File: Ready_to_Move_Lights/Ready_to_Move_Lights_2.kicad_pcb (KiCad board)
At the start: 2 copper layers, 81.3 x 81.3 mm, 46 parts, among them IC1 TLV2371QDBVRQ1, J1 PET-02-XX-X-VT-LC, J2 776280-1, K1 VORA1150-X017T, Q1 IRLZ44N, U1 LM393LVQDDFRQ1, U2 PAMC0381D10QDFXRQ1, U3 NE555D

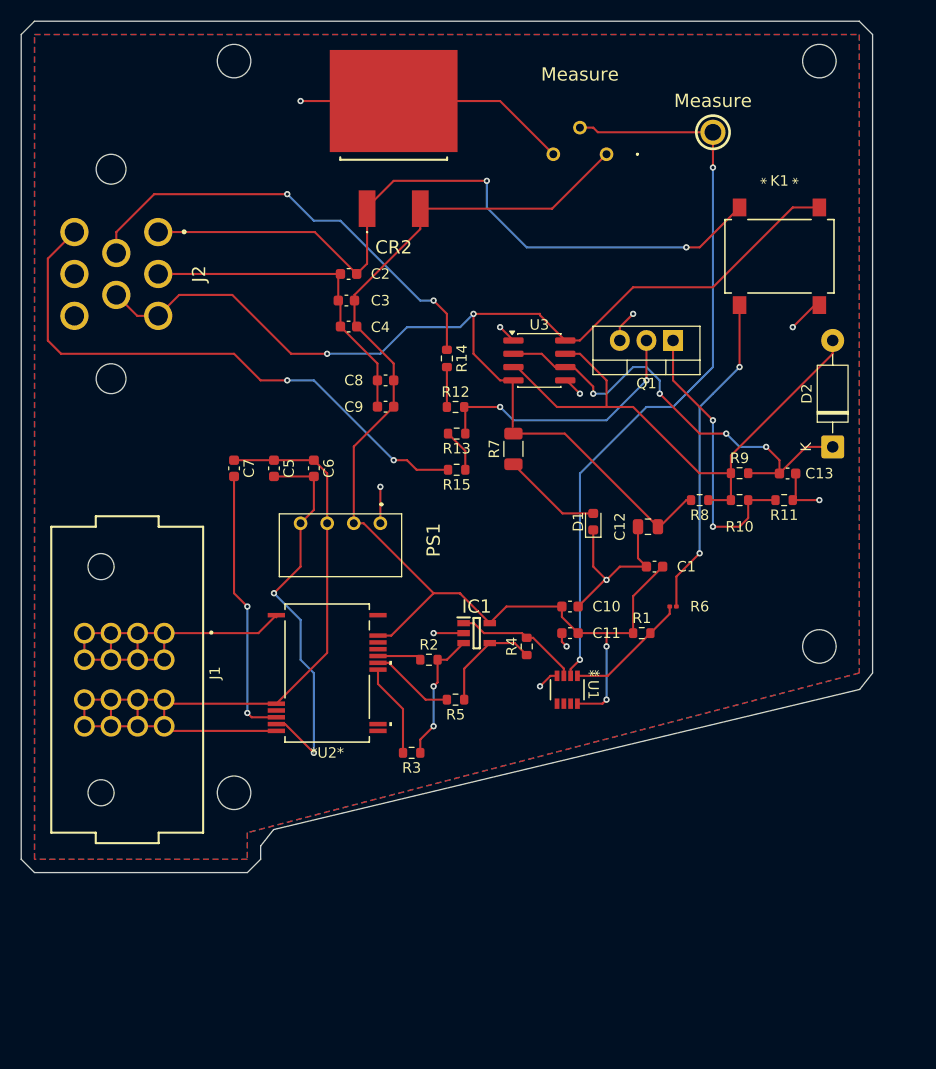
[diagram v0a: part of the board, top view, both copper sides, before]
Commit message: Ready_to_Move_Lights Changes
Fixed accidental wiring on 555 output, changed lights' resistors, compressed whole PCB, improved decoupling cap placement
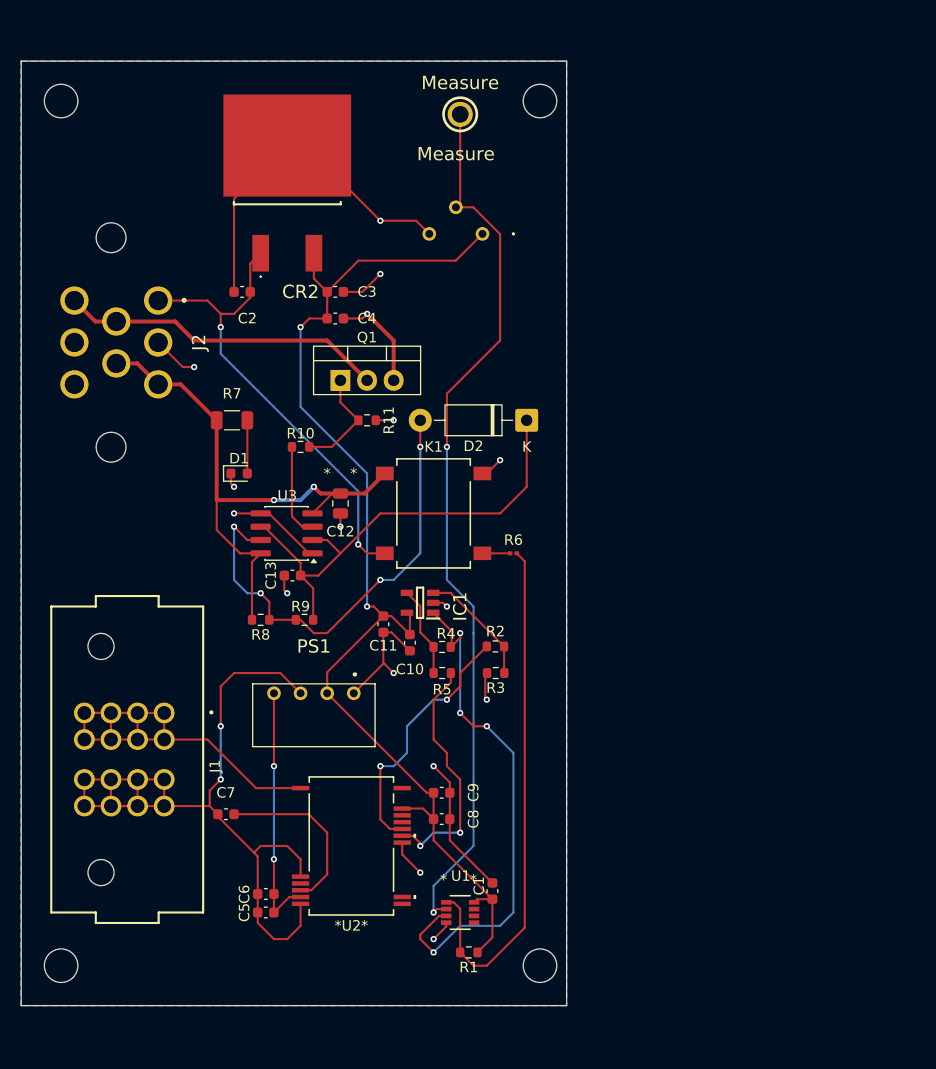
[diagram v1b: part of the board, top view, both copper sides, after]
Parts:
- removed the ? at (118.1, 40.6)
- removed the ? at (174.0, 40.6)
- removed the ? at (174.0, 96.5)
- removed the ? at (118.1, 110.5)
- removed R12, R13: 25, Resistor_SMD:R_0603_1608Metric
- removed R14, R15: 100, Resistor_SMD:R_0603_1608Metric
- added ?: , , F.Cu at (101.6, 44.5)
- added ?: , , F.Cu at (101.6, 127.0)
- added ?: , , F.Cu at (147.3, 44.5)
- added ?: , , F.Cu at (147.3, 127.0)
- moved C13 48.3 mm to (123.7, 89.8), turned to 180 degrees
- moved R9 43.8 mm to (124.8, 94.0)
- moved R8 43.4 mm to (120.7, 94.0)
- moved C5 42.4 mm to (121.1, 121.9), turned to 0 degrees
- moved C8 42.2 mm to (137.9, 113.0), turned to 180 degrees
- moved R10 42.2 mm to (124.5, 77.5)
- moved K1 41.1 mm to (137.2, 83.8), turned to 180 degrees
- moved C6 40.9 mm to (121.1, 120.2), turned to 0 degrees
- moved R11 40.5 mm to (130.8, 74.9)
- moved C9 37.2 mm to (137.9, 110.5), turned to 180 degrees
- moved R1 34.7 mm to (140.5, 125.7), turned to 180 degrees
- moved C1 34.6 mm to (142.8, 119.9), turned to 90 degrees
- moved D1 34.1 mm to (118.6, 80.0), turned to 0 degrees
- moved C7 33.0 mm to (117.3, 112.5), turned to 0 degrees
- moved Q1 32.0 mm to (128.3, 71.1), turned to 0 degrees
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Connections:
- J2 pad 6: /Light2GND -> /Light1GND
- Q1 pad 2: Net-(Q1-D) -> /Light1GND
- R10 pad 1: Net-(D2-A) -> Net-(U3-Q)
- U3 pad 3: Net-(D2-A) -> Net-(U3-Q)
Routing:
- net /Light1+: track 113.9 -> 55.2 mm
- net /Light2GND: track 54.7 -> 0.00 mm, vias 2 -> 0
- net /V_IND: track 12.0 -> 50.0 mm
- net /V_OUT: track 12.1 -> 49.7 mm, vias 0 -> 4
- net Net-(K1-Pad1): track 31.3 -> 2.64 mm, vias 2 -> 0
- net Net-(Q1-D): track 25.9 -> 0.00 mm, vias 2 -> 0
- net /12V Master: track 69.7 -> 44.9 mm
- net /OUT_P: track 4.19 -> 24.7 mm, vias 0 -> 2
- net Net-(Q1-G): track 27.4 -> 10.3 mm, vias 2 -> 0
- net /OUT_N: track 8.03 -> 23.6 mm, vias 0 -> 2
- net +5VDD: track 38.1 -> 24.1 mm
- net /V_LOW_REF: track 71.9 -> 85.2 mm
- net /Light1GND: track 43.2 -> 31.1 mm, vias 2 -> 0
- net 01: track 37.0 -> 48.0 mm
- net Net-(U2-SNSP): track 26.0 -> 16.8 mm, vias 2 -> 0
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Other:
- board size 81.3 x 81.3 mm -> 52.1 x 90.2 mm
